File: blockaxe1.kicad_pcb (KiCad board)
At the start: 4 copper layers, 56.5 x 99.8 mm, 138 parts, among them J1 TC2030-IDC, J2 TC2030-IDC, J3 Conn_01x04, J4 USB_C_Receptacle_USB2.0, J5 54-00164, J6 Conn_01x04, Q4 CSD17575Q3, Q5 CSD17312Q5, SW1 EVQ-9P701P, SW2 EVQ-9P701P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

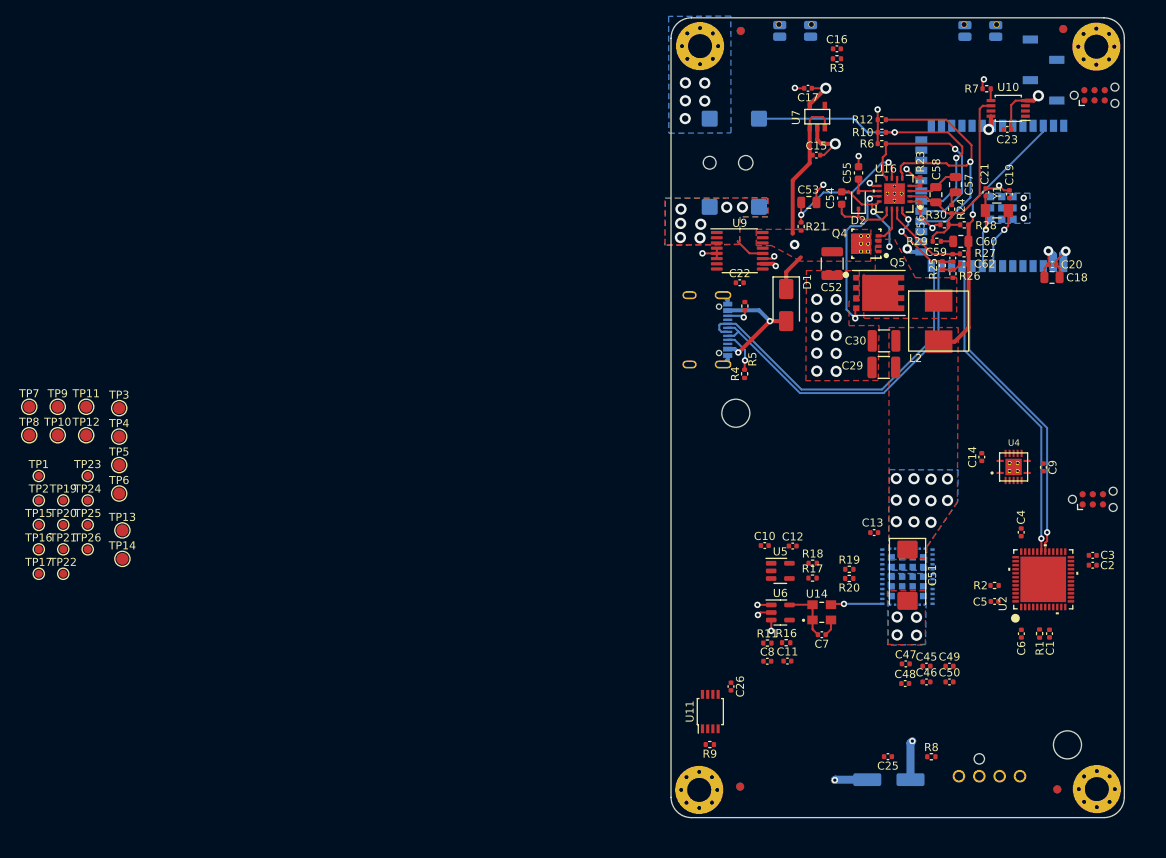
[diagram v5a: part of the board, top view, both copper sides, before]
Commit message: finished routing. switched back to THT barrel
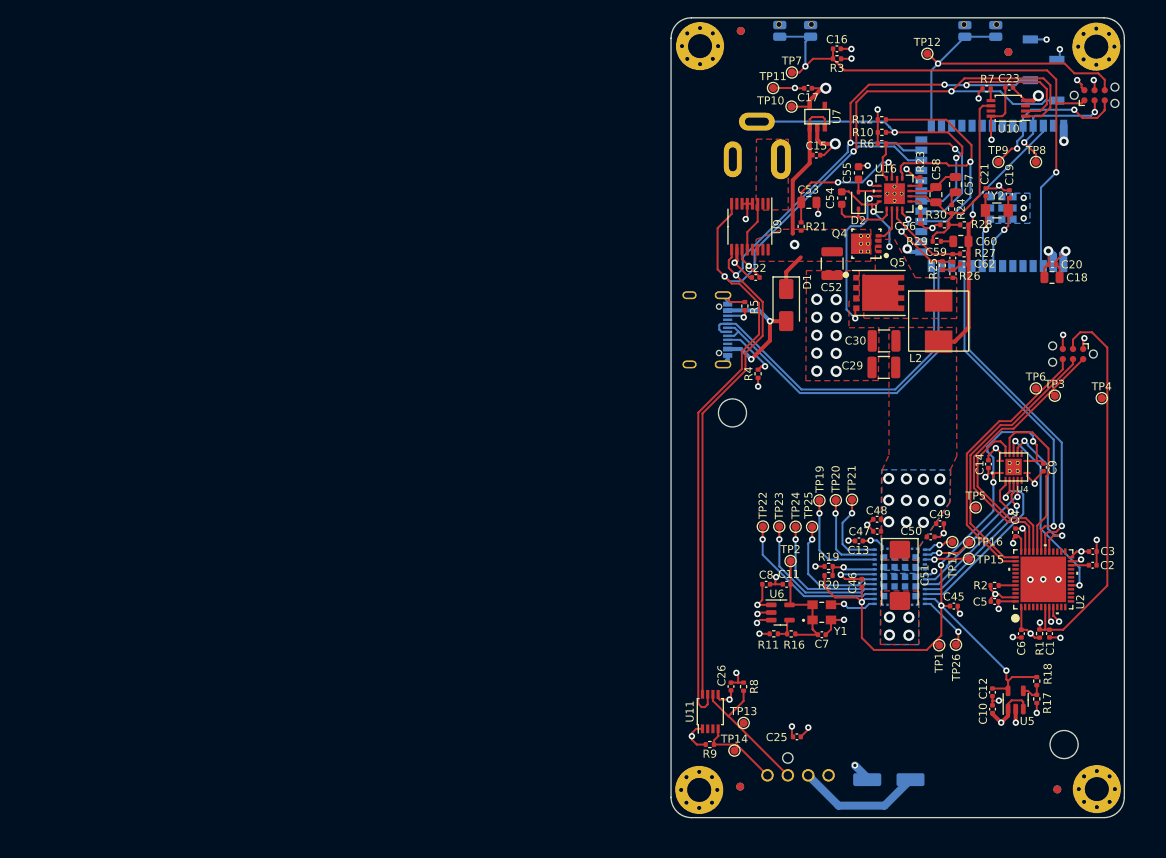
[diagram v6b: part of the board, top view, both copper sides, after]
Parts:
- J5: value 54-00164 -> PJ-002B; footprint blockaxe:BarrelJack_Wuerth_694106106102_2.0x5.5mm -> blockaxe:CUI_PJ-002B
- TP10, TP11, TP12, TP13, TP14, TP3, TP4, TP5, TP6, TP7, TP8, TP9: footprint TestPoint:TestPoint_Pad_D1.5mm -> TestPoint:TestPoint_Pad_D1.0mm
- moved TP8 130.1 mm to (149.3, 64.6)
- moved TP4 122.7 mm to (157.5, 94.1)
- moved TP9 121.2 mm to (144.6, 64.6)
- moved TP3 116.7 mm to (151.6, 93.8)
- moved TP15 116.1 mm to (140.9, 114.1)
- moved TP16 116.1 mm to (140.9, 112.1)
- moved TP12 115.2 mm to (135.7, 51.1)
- moved TP6 115.1 mm to (149.2, 92.9)
- moved TP1 114.3 mm to (137.2, 124.9)
- moved TP17 114.0 mm to (138.8, 112.0)
- moved TP26 109.0 mm to (139.3, 124.8)
- moved TP5 107.0 mm to (141.8, 107.7)
- moved TP7 103.9 mm to (118.8, 53.5)
- moved TP10 100.3 mm to (118.8, 57.7)
- moved TP21 98.6 mm to (126.3, 106.8)
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- renumbered U14 to Y1, Y1 to Y2
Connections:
- C1 pad 1: /STM32/RESET -> /STM32/SWRESET
- C26 pad 1: /Fan/3V3 -> VDD
- C9 pad 1: /ASIC/1V8 -> /ASIC/1V2
- J1 pad 3: /STM32/RESET -> /STM32/SWRESET
- R1 pad 1: /STM32/RESET -> /STM32/SWRESET
- R8 pad 2: /Fan/3V3 -> VDD
- R9 pad 2: /Fan/3V3 -> VDD
- TP4 pad 1: /STM32/RESET -> /STM32/SWRESET
- U1 pad 18: /ASIC/TX_OUT -> /ASIC/RX_IN
- U11 pad 1: /Fan/3V3 -> VDD
- U2 pad 17: /STM32/RESET -> /ASIC/RST
- U2 pad 7: /STM32/RESET -> /STM32/SWRESET
- U4 pad 1: /ASIC/1V8 -> /ASIC/1V2
- U4 pad 11: /STM32/RESET -> /ASIC/RST
- U4 pad 8: /ASIC/1V8 -> /ASIC/1V2
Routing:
- net /SDA: track 0.00 -> 157.8 mm, vias 0 -> 3
- net /SCL: track 0.00 -> 136.3 mm, vias 0 -> 4
- net /ASIC/1V2: track 0.00 -> 91.1 mm, vias 0 -> 6
- net GND: track 54.2 -> 139.5 mm, vias 37 -> 65
- net /ESP32/EN: track 0.00 -> 71.7 mm, vias 0 -> 2
- net VDD: track 21.9 -> 80.3 mm, vias 8 -> 21
- net /STM32/SWRESET: track 0.00 -> 51.5 mm, vias 0 -> 1
- net /ESP32/IO0: track 0.00 -> 41.5 mm, vias 0 -> 1
- net /STM32/SWDIO: track 0.00 -> 35.3 mm
- net /STM32/SWO: track 0.00 -> 35.1 mm
- net /STM32/SWCLK: track 0.00 -> 34.7 mm
- net /ASIC/RX_IN: track 0.00 -> 24.0 mm, vias 0 -> 1
- net /ASIC/RST: track 0.00 -> 24.0 mm, vias 0 -> 2
- net /STM32/TX6: track 0.00 -> 21.4 mm
- net /STM32/RX6: track 0.00 -> 21.2 mm
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- removed copper zone on B.Cu, net /Power/VIN
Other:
- board text added: "5VDC"

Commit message: added gerbers and BOM
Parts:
- added J7: Conn_01x03, Connector_PinHeader_2.54mm:PinHeader_1x03_P2.54mm_Vertical, B.Cu at (157.9, 125.0)
- C54: value 220nF -> 0.22uF
- C55: footprint Capacitor_SMD:C_0603_1608Metric -> Capacitor_SMD:C_0805_2012Metric
- C56: value 27nF -> 0.027uF
- C57: value 1nF -> 0.001uF
- C62: value 220nF -> 0.22uF; footprint Capacitor_SMD:C_0402_1005Metric -> Capacitor_SMD:C_0603_1608Metric
- G***, J1, J2: moved to B.Cu
- moved G*** 110.1 mm to (131.5, 90.1), turned to 180 degrees
- moved J2 28.3 mm to (153.9, 84.5), turned to 180 degrees
- moved FID5 12.1 mm to (157.0, 55.6)
- moved FID7 12.1 mm to (157.0, 55.6)
- moved FID1 8.99 mm to (107.3, 55.7)
- moved FID3 8.99 mm to (107.3, 55.7)
- moved J6 7.54 mm to (115.9, 141.8), turned to 0 degrees
- moved TP4 5.25 mm to (155.7, 99.0)
- moved J1 3.04 mm to (153.9, 91.6)
- moved TP6 2.27 mm to (148.1, 90.9)
- moved TP3 2.11 mm to (149.6, 94.4)
- moved TP9 2.03 mm to (146.3, 63.5)
- moved C25 1.85 mm to (118.7, 134.6), turned to 0 degrees
- moved C30 0.85 mm to (129.5, 86.9)
- moved C29 0.81 mm to (129.5, 90.3)
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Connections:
- U2 pad 12: unconnected-(U2-PA2-Pad12) -> /STM32/TX2
- U2 pad 13: unconnected-(U2-PA3-Pad13) -> /STM32/RX2
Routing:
- net /ESP32/IO0: track 41.5 -> 68.3 mm, vias 1 -> 2
- net /ESP32/P_TX: track 16.0 -> 36.3 mm
- net /ESP32/EN: track 71.7 -> 88.8 mm, vias 2 -> 3
- net /ESP32/P_RX: track 19.8 -> 36.3 mm
- net /STM32/TX2: track 0.00 -> 12.3 mm, vias 0 -> 1
- net /Fan/FAN_PWM: track 11.4 -> 23.3 mm
- net /STM32/RX2: track 0.00 -> 9.10 mm, vias 0 -> 1
- net /STM32/SWRESET: track 51.5 -> 42.7 mm
- net /5V: track 112.8 -> 119.9 mm
- net /STM32/SWO: track 35.1 -> 40.2 mm, vias 0 -> 1
- net GND: track 139.5 -> 144.5 mm
- net /VDD: track 33.7 -> 38.2 mm
- net /STM32/SWCLK: track 34.7 -> 39.0 mm, vias 0 -> 1
- net /STM32/SWDIO: track 35.3 -> 38.9 mm, vias 0 -> 1
- net /Fan/FAN_TACH: track 18.7 -> 21.7 mm
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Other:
- board text added: "100"
- board text added: "ESP"
- board text added: "GND"
- board text added: "RXO"
- board text added: "STM"
- board text added: "TXI"

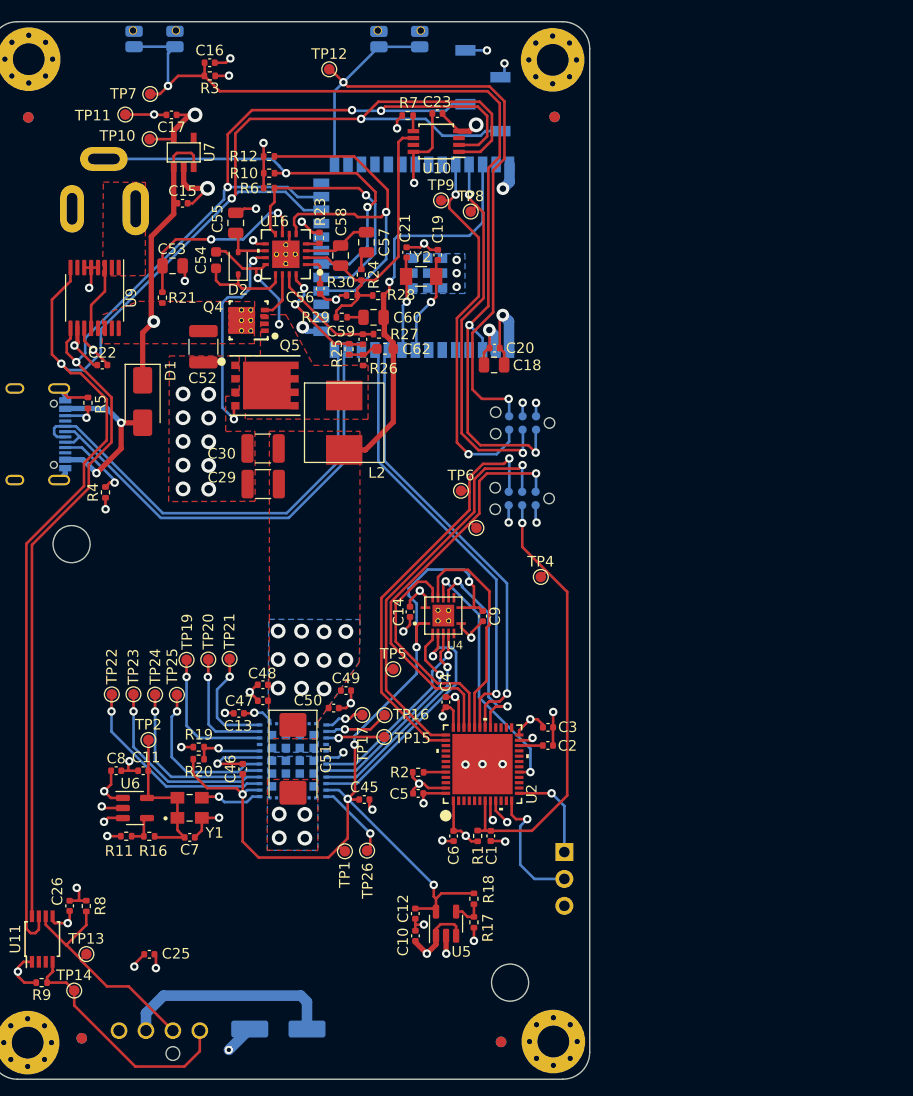
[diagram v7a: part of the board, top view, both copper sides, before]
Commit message: changed buttons for #5 flipped display for #2
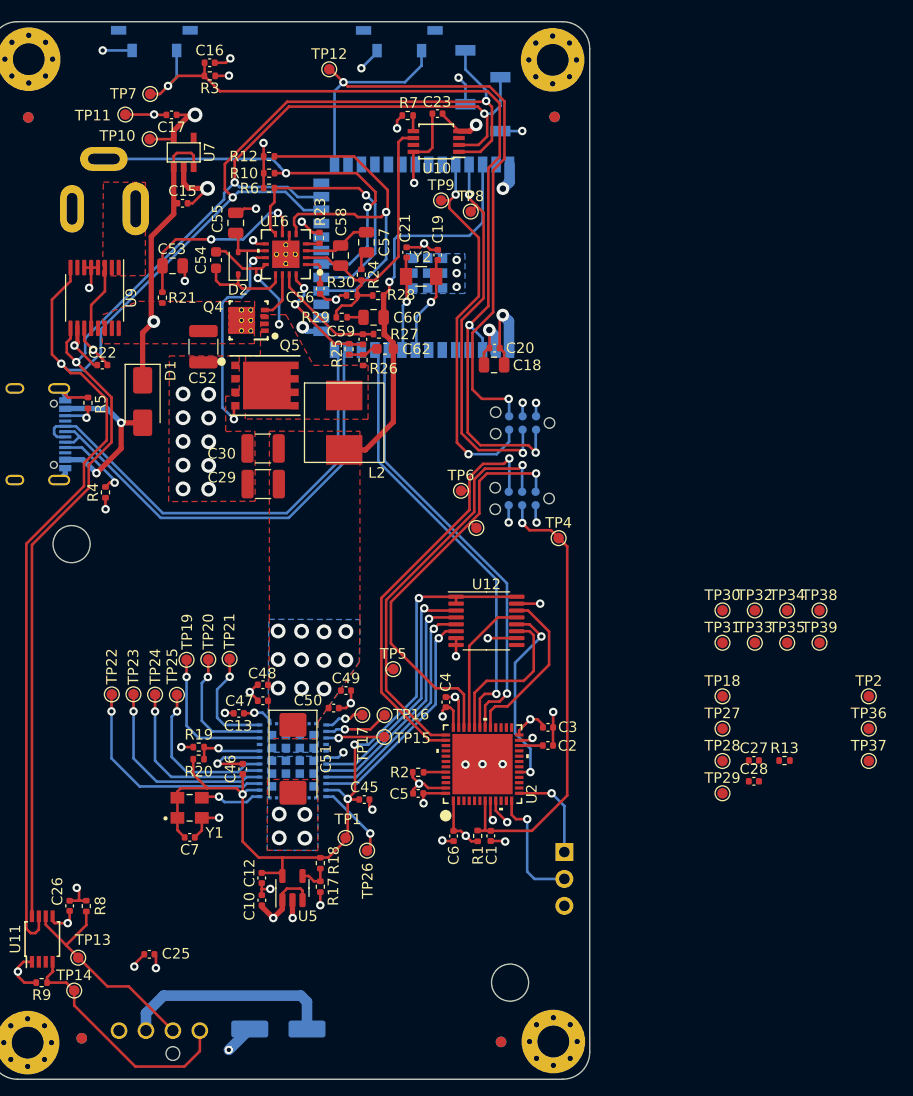
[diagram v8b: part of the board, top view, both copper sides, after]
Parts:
- removed C11: 1uF, Capacitor_SMD:C_0402_1005Metric
- removed C14, C8, C9: 0.1uF, Capacitor_SMD:C_0402_1005Metric
- removed R11: 78.7k 1%, Resistor_SMD:R_0402_1005Metric
- removed R16: 182k 1%, Resistor_SMD:R_0402_1005Metric
- removed U4: TXB0104RGYR, blockaxe:TXB0104
- removed U6: ADP171AUJ-R7, Package_TO_SOT_SMD:TSOT-23-5
- added C27: 311-3342-1-ND, Capacitor_SMD:C_0402_1005Metric, F.Cu at (175.8, 116.3)
- added C28: 311-3342-1-ND, Capacitor_SMD:C_0402_1005Metric, F.Cu at (175.8, 118.3)
- added R13: 20k, Resistor_SMD:R_0402_1005Metric, F.Cu at (178.7, 116.3)
- added TP18: TestPoint, TestPoint:TestPoint_Pad_D1.0mm, F.Cu at (172.8, 110.3)
- added TP27: TestPoint, TestPoint:TestPoint_Pad_D1.0mm, F.Cu at (172.8, 113.3)
- added TP28: TestPoint, TestPoint:TestPoint_Pad_D1.0mm, F.Cu at (172.8, 116.4)
- added TP29: TestPoint, TestPoint:TestPoint_Pad_D1.0mm, F.Cu at (172.8, 119.4)
- added TP30: TestPoint, TestPoint:TestPoint_Pad_D1.0mm, F.Cu at (172.8, 102.2)
- added TP31: TestPoint, TestPoint:TestPoint_Pad_D1.0mm, F.Cu at (172.8, 105.2)
- added TP32: TestPoint, TestPoint:TestPoint_Pad_D1.0mm, F.Cu at (175.9, 102.2)
- added TP33: TestPoint, TestPoint:TestPoint_Pad_D1.0mm, F.Cu at (175.9, 105.2)
- added TP34: TestPoint, TestPoint:TestPoint_Pad_D1.0mm, F.Cu at (178.9, 102.2)
- added TP35: TestPoint, TestPoint:TestPoint_Pad_D1.0mm, F.Cu at (178.9, 105.2)
- added TP36: TestPoint, TestPoint:TestPoint_Pad_D1.0mm, F.Cu at (186.6, 113.3)
- added TP37: TestPoint, TestPoint:TestPoint_Pad_D1.0mm, F.Cu at (186.6, 116.4)
- added TP38: TestPoint, TestPoint:TestPoint_Pad_D1.0mm, F.Cu at (182.0, 102.2)
- added TP39: TestPoint, TestPoint:TestPoint_Pad_D1.0mm, F.Cu at (182.0, 105.2)
- added U12: SN74AVC4T774, Package_SO:TSSOP-16_4.4x5mm_P0.65mm, F.Cu at (150.5, 103.2)
- SW1, SW2: value EVQ-9P701P -> TL3330AF260QG; footprint blockaxe:EVQ9P701P-switch -> blockaxe:SW_TL3330_EWI
- moved TP2 68.1 mm to (186.6, 110.3)
- moved C12 14.9 mm to (129.3, 127.4)
- moved R18 14.9 mm to (134.9, 126.0)
- moved C10 14.9 mm to (129.3, 129.5)
- moved R17 14.9 mm to (134.9, 128.2)
- moved U5 14.9 mm to (132.2, 128.4)
- moved TP4 4.03 mm to (157.3, 95.4)
- moved TP1 1.26 mm to (137.2, 123.6)
- moved TP13 0.84 mm to (112.0, 134.9)
- moved SW2 0.20 mm to (142.3, 48.5), turned to 0 degrees
- moved SW1 0.19 mm to (119.2, 48.5), turned to 0 degrees
- turned J3 to 0 degrees
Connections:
- net /Power/VIN renamed IN+
- net /VDD renamed /COREV
- C10 pad 1: VDD -> /3V3
- C17 pad 1: VDD -> /3V3
- C18 pad 1: VDD -> /3V3
- C20 pad 1: VDD -> /3V3
- C22 pad 1: VDD -> /3V3
- C23 pad 1: VDD -> /3V3
- C26 pad 1: VDD -> /3V3
- C7 pad 2: /ASIC/1V65 -> /ASIC/1V2
- J2 pad 2: VDD -> /3V3
- J3 pad 2: VDD -> /3V3
- R10 pad 1: VDD -> /3V3
- R12 pad 1: VDD -> /3V3
- R3 pad 1: VDD -> /3V3
- R6 pad 1: VDD -> /3V3
- R8 pad 2: VDD -> /3V3
- R9 pad 2: VDD -> /3V3
- TP10 pad 1: VDD -> /3V3
- TP2 pad 1: /ASIC/1V65 -> /PWR_EN
- U10 pad 8: VDD -> /3V3
- U11 pad 1: VDD -> /3V3
- U2 pad 17: /ASIC/RST -> /STM32/RESET
- U2 pad 29: /ASIC/TRIP -> /STM32/TRIP
- U5 pad 1: VDD -> /3V3
- U5 pad 3: VDD -> /3V3
- U7 pad 5: VDD -> /3V3
- U8 pad 15: VDD -> /3V3
- U8 pad 2: VDD -> /3V3
- U9 pad 10: VDD -> /3V3
- Y1 pad 1: /ASIC/1V65 -> /ASIC/1V2
- Y1 pad 4: /ASIC/1V65 -> /ASIC/1V2
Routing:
- net VDD: track 81.0 -> 20.0 mm, vias 21 -> 6
- net /3V3: track 0.00 -> 54.7 mm, vias 0 -> 13
- net /ASIC/RST: track 24.0 -> 0.00 mm, vias 2 -> 0
- net /ASIC/TRIP: track 19.5 -> 0.00 mm, vias 2 -> 0
- net /STM32/RESET: track 0.00 -> 18.3 mm, vias 0 -> 2
- net /STM32/TRIP: track 0.00 -> 15.9 mm
- net /ASIC/1V65: track 15.3 -> 0.00 mm
- net /ASIC/1V2: track 92.1 -> 77.4 mm, vias 6 -> 4
- net /SDA: track 157.6 -> 149.0 mm
- net /STM32/RX6: track 21.2 -> 13.3 mm
- net /STM32/TX6: track 21.4 -> 14.8 mm
- net /SCL: track 136.3 -> 130.7 mm, vias 4 -> 3
- net /ASIC/TRIP_OUT: track 18.7 -> 23.3 mm
- net /ESP32/EN: track 88.8 -> 84.7 mm
- net Net-(U6-ADJ): track 3.00 -> 0.00 mm
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- added copper zone on In2.Cu, net /3V3
- removed copper zone on In2.Cu, net VDD
